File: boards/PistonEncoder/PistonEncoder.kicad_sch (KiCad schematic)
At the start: 12 parts

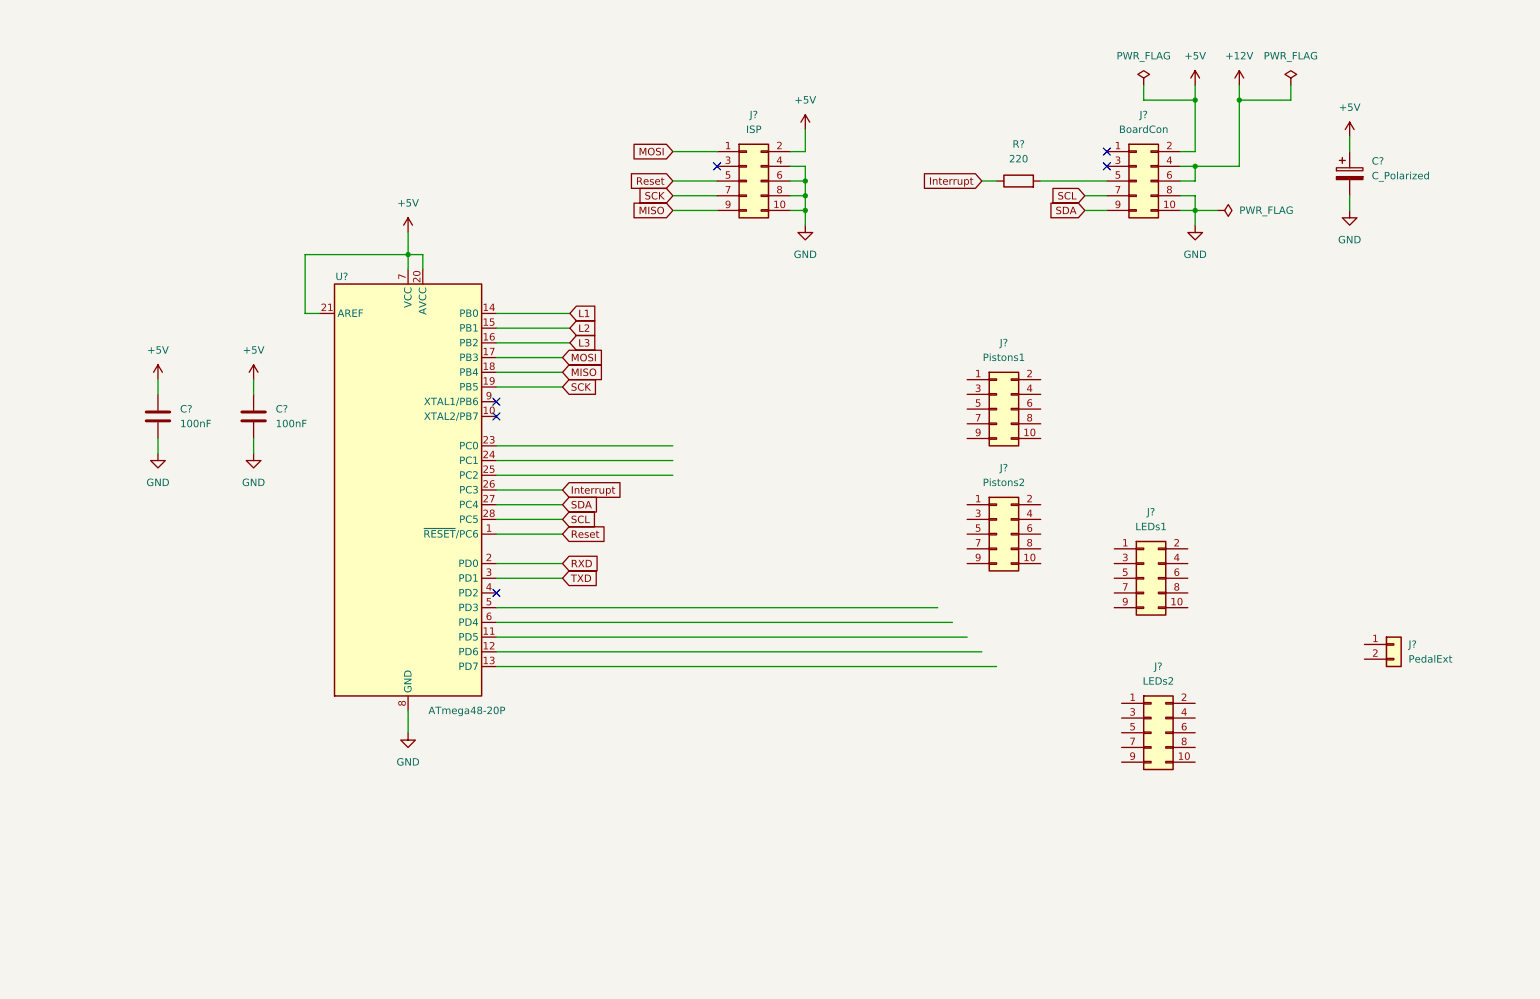
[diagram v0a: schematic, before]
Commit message: Some updates to piston encoder schematics
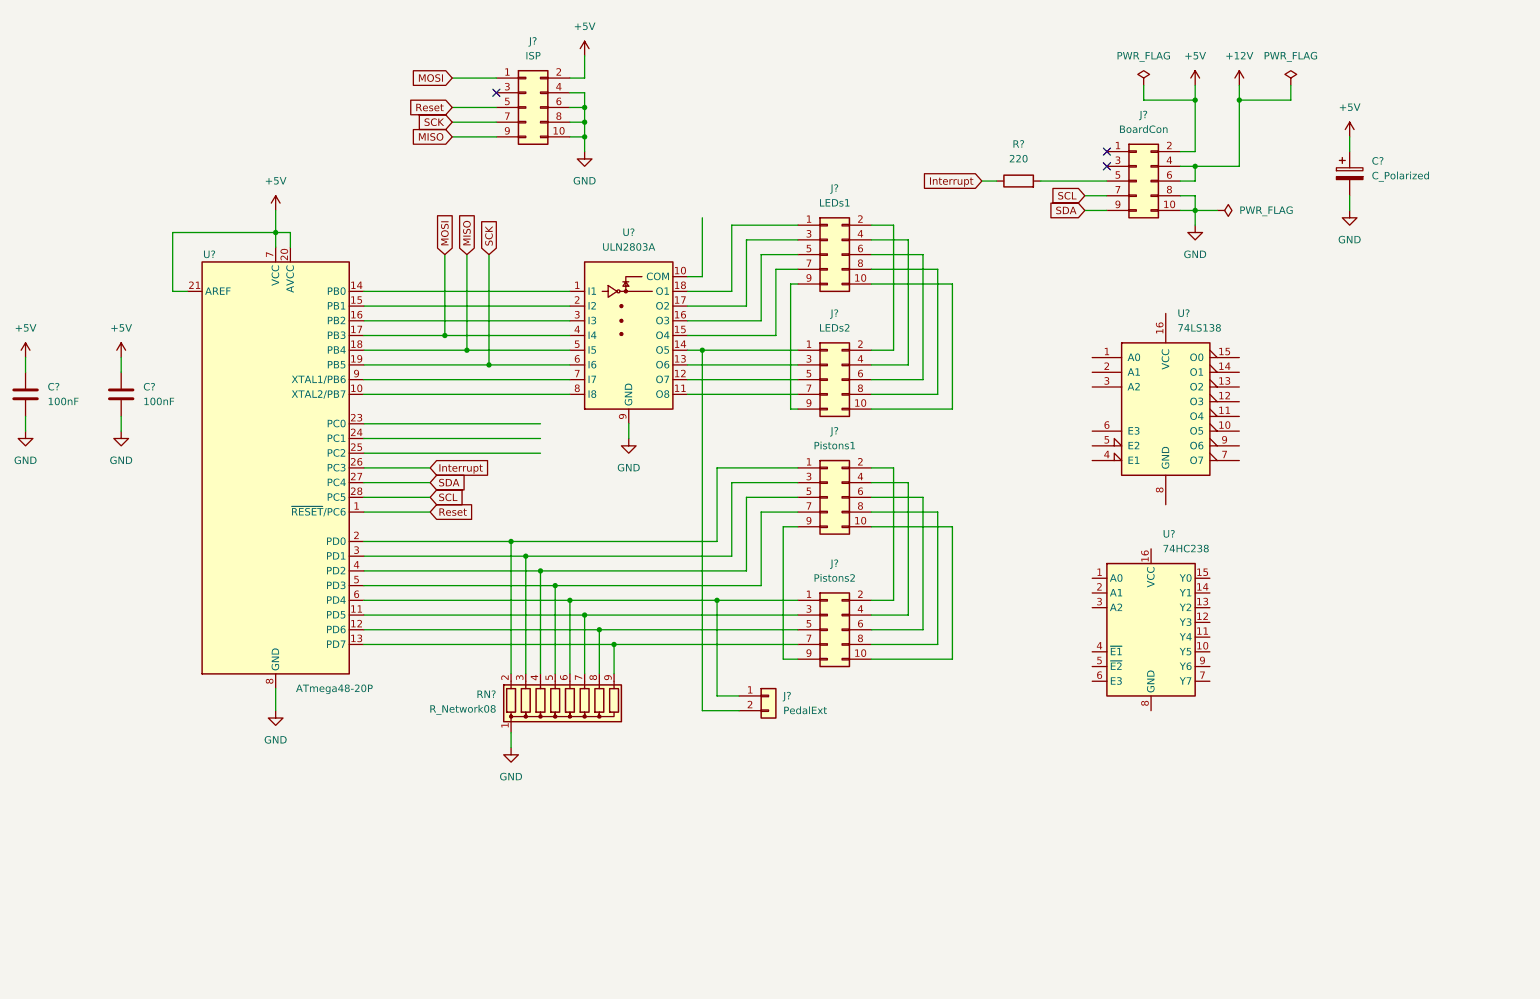
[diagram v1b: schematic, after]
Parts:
- added RN?: R_Network08, Resistor_THT:R_Array_SIP9, symbol Device:R_Network08
- added U?: ULN2803A, symbol Transistor_Array:ULN2803A
- added U?: 74HC238, symbol 74xx:74HC238
- added U?: 74LS138, symbol 74xx:74LS138
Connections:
- net RXD is gone; now on an unnamed net: U?.2 (PD0)
- net TXD is gone; now on an unnamed net: U?.3 (PD1)
- net GND: now also RN?.1 (common), U?.9 (GND)
- net MISO: now also U?.5 (I5)
- net MOSI: now also U?.4 (I4)
- net SCK: now also U?.6 (I6)
- net at J?.1 (Pin_1): now also U?.18 (O1)
- net at J?.10 (Pin_10): now also J?.10 (Pin_10) (x2)
- net at J?.2 (Pin_2): now also J?.2 (Pin_2) (x2)
- net at J?.3 (Pin_3): now also U?.17 (O2)
- net at J?.4 (Pin_4): now also J?.4 (Pin_4) (x2)
- net at J?.5 (Pin_5): now also U?.16 (O3)
- net at J?.6 (Pin_6): now also J?.6 (Pin_6) (x2)
- net at J?.7 (Pin_7): now also U?.15 (O4)
- net at J?.8 (Pin_8): now also J?.8 (Pin_8) (x2)
- net at J?.9 (Pin_9): now also J?.9 (Pin_9) (x2)
- net at J?.1 (Pin_1): now also J?.2 (Pin_2), U?.14 (O5)
- net at J?.3 (Pin_3): now also U?.13 (O6)
- net at J?.5 (Pin_5): now also U?.12 (O7)
- net at J?.7 (Pin_7): now also U?.11 (O8)
- net at U?.10 (XTAL2/PB7): now also U?.8 (I8)
- net at U?.11 (PD5): now also J?.3 (Pin_3), RN?.7 (R6)
- net at U?.12 (PD6): now also J?.5 (Pin_5), RN?.8 (R7)
- net at U?.13 (PD7): now also J?.7 (Pin_7), RN?.9 (R8)
- net at U?.4 (PD2): now also J?.5 (Pin_5), RN?.4 (R3)
- net at U?.5 (PD3): now also J?.7 (Pin_7), RN?.5 (R4)
- net at U?.6 (PD4): now also J?.1 (Pin_1), J?.1 (Pin_1), RN?.6 (R5)
- net at U?.9 (XTAL1/PB6): now also U?.7 (I7)
- net at J?.1 (Pin_1): now also RN?.2 (R1)
- net at J?.3 (Pin_3): now also RN?.3 (R2)
- net L1: no longer names the net of U?.14 (PB0)
- net L1: now also U?.1 (I1)
- net L2: no longer names the net of U?.15 (PB1)
- net L2: now also U?.2 (I2)
- net L3: no longer names the net of U?.16 (PB2)
- net L3: now also U?.3 (I3)
- no-connect marks 6 -> 3
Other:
- moved on the sheet: C?, J?, U?

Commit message: Finished Piston encoder schematics
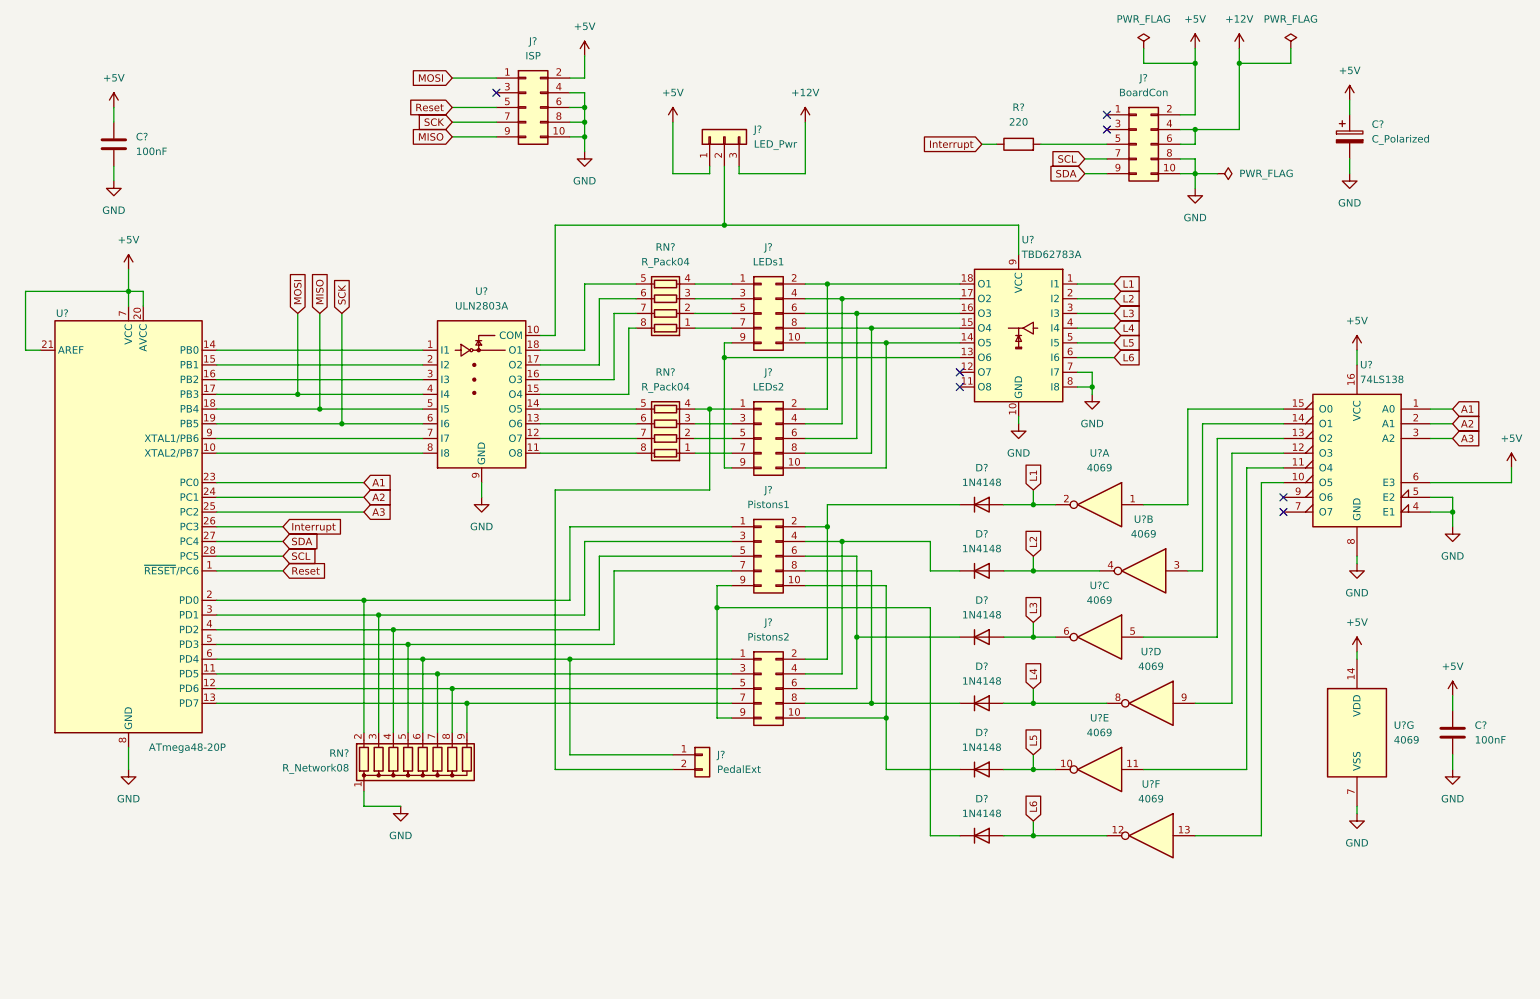
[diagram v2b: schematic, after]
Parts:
- removed U?: 74HC238, symbol 74xx:74HC238
- added D? (x6): 1N4148, Diode_THT:D_DO-35_SOD27_P7.62mm_Horizontal, symbol Diode:1N4148
- added J?: LED_Pwr, symbol Connector_Generic:Conn_01x03
- added RN? (x2): R_Pack04, symbol Device:R_Pack04
- added U? (x7): 4069, symbol 4xxx:4069
- added U?: TBD62783A, symbol Transistor_Array:TBD62783A
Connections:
- net +12V: now also J?.3 (Pin_3)
- net +5V: now also U?.16 (VCC), U?.6 (E3), J?.1 (Pin_1), U?.14 (VDD)
- net GND: now also U?.4 (E1), U?.5 (E2), U?.8 (GND), U?.10 (GND), U?.7 (I7), U?.7 (VSS), U?.8 (I8)
- net at J?.1 (Pin_1): now also RN?.4 (R4.1); no longer U?.18 (O1)
- net at J?.10 (Pin_10), J?.10 (Pin_10): now also U?.14 (O5)
- net at J?.2 (Pin_2), J?.2 (Pin_2): now also U?.18 (O1)
- net at J?.3 (Pin_3): now also RN?.3 (R3.1); no longer U?.17 (O2)
- net at J?.4 (Pin_4), J?.4 (Pin_4): now also U?.17 (O2)
- net at J?.5 (Pin_5): now also RN?.2 (R2.1); no longer U?.16 (O3)
- net at J?.6 (Pin_6), J?.6 (Pin_6): now also U?.16 (O3)
- net at J?.7 (Pin_7): now also RN?.1 (R1.1); no longer U?.15 (O4)
- net at J?.8 (Pin_8), J?.8 (Pin_8): now also U?.15 (O4)
- net at J?.9 (Pin_9), J?.9 (Pin_9): now also U?.13 (O6)
- net at U?.10 (COM): now also J?.2 (Pin_2), U?.9 (VCC)
- net at U?.11 (O8): now also RN?.8 (R1.2); no longer J?.7 (Pin_7)
- net at U?.12 (O7): now also RN?.7 (R2.2); no longer J?.5 (Pin_5)
- net at U?.13 (O6): now also RN?.6 (R3.2); no longer J?.3 (Pin_3)
- net at J?.1 (Pin_1), J?.2 (Pin_2): now also RN?.4 (R4.1); no longer U?.14 (O5)
- net A1: now reaches U?.23 (PC0)
- net A1: now also U?.1 (A0)
- net A2: now reaches U?.24 (PC1)
- net A2: now also U?.2 (A1)
- net A3: now reaches U?.25 (PC2)
- net A3: now also U?.3 (A2)
- net at J?.10 (Pin_10), J?.10 (Pin_10): now also D?.1 (K)
- net at J?.2 (Pin_2), J?.2 (Pin_2): now also D?.1 (K)
- net at J?.4 (Pin_4), J?.4 (Pin_4): now also D?.1 (K)
- net at J?.6 (Pin_6), J?.6 (Pin_6): now also D?.1 (K)
- net at J?.8 (Pin_8), J?.8 (Pin_8): now also D?.1 (K)
- net at J?.9 (Pin_9), J?.9 (Pin_9): now also D?.1 (K)
- net at U?.10 (O5): now also U?.13
- net at U?.11 (O4): now also U?.11
- net at U?.12 (O3): now also U?.9
- net at U?.13 (O2): now also U?.5
- net at U?.14 (O1): now also U?.3
- net at U?.15 (O0): now also U?.1
- new net: RN?.5 (R4.2), U?.14 (O5)
- new net: RN?.8 (R1.2), U?.15 (O4)
- new net: RN?.7 (R2.2), U?.16 (O3)
- new net: RN?.6 (R3.2), U?.17 (O2)
- new net: RN?.5 (R4.2), U?.18 (O1)
- new net: J?.3 (Pin_3), RN?.3 (R3.1)
- new net: J?.5 (Pin_5), RN?.2 (R2.1)
- new net: J?.7 (Pin_7), RN?.1 (R1.1)
- new net L1: D?.2 (A), U?.1 (I1), U?.2
- new net L2: D?.2 (A), U?.2 (I2), U?.4
- new net L3: D?.2 (A), U?.3 (I3), U?.6
- new net L4: D?.2 (A), U?.4 (I4), U?.8
- new net L5: D?.2 (A), U?.10, U?.5 (I5)
- new net L6: D?.2 (A), U?.12, U?.6 (I6)
- no-connect marks 3 -> 7
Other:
- moved on the sheet: C?, J?, R?, RN?, U?

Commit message: Renamed PCBs and updated to KiCAD 7.0
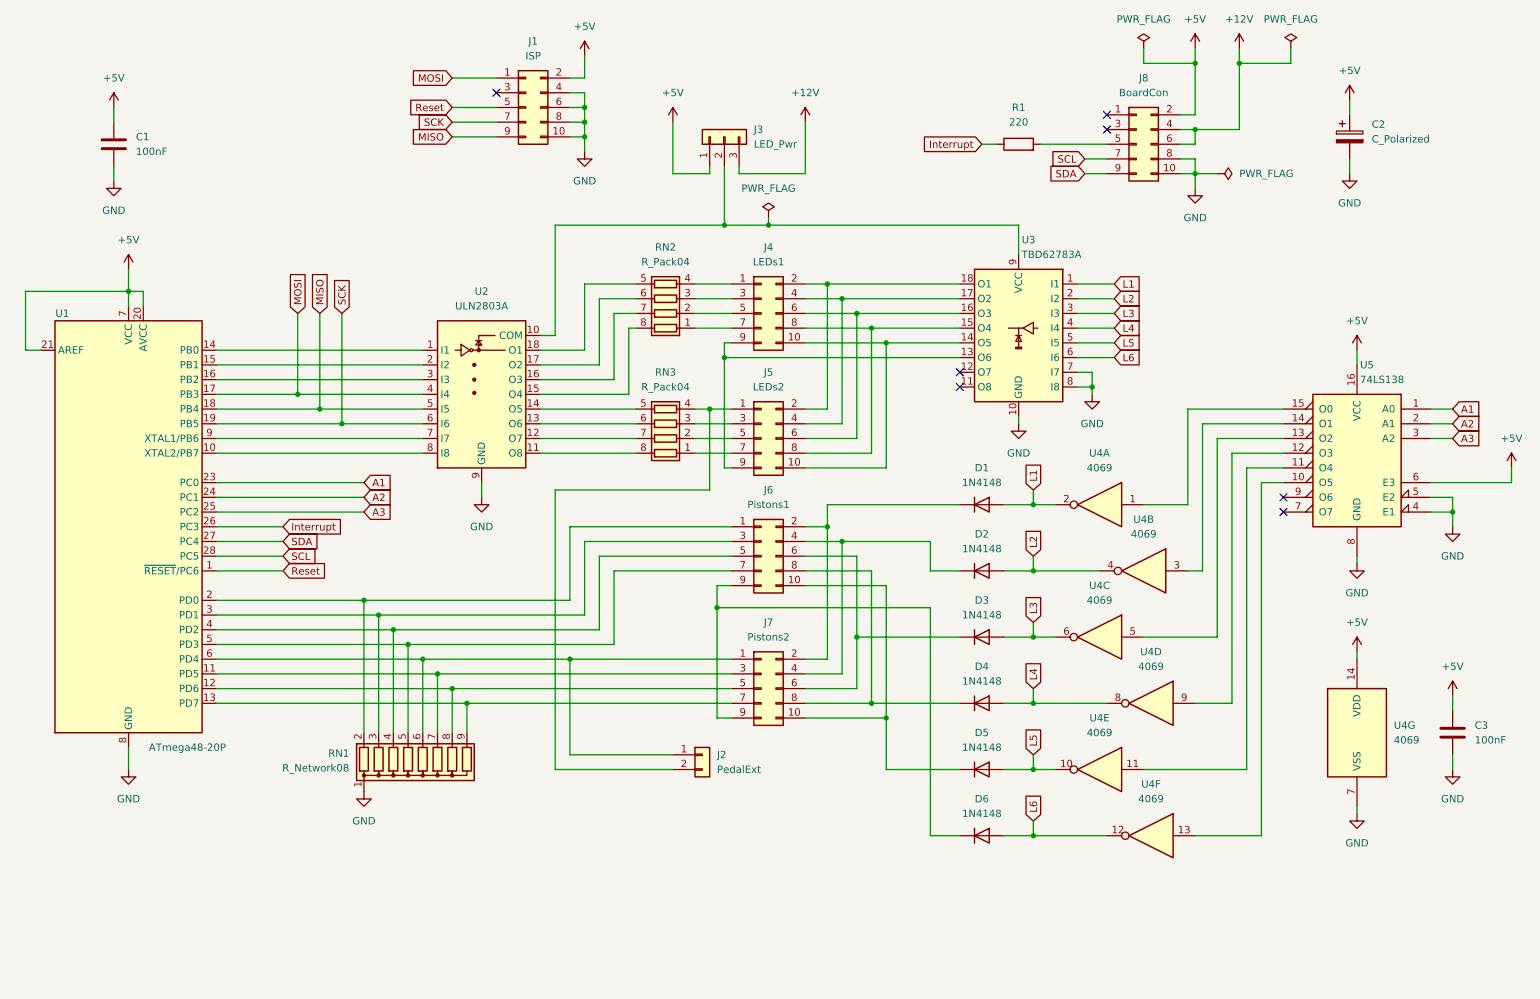
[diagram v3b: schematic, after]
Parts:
- C1: renamed from C?; footprint (none) -> Capacitor_THT:C_Disc_D7.5mm_W2.5mm_P5.00mm
- C2: renamed from C?; footprint (none) -> Capacitor_THT:CP_Radial_D10.0mm_P5.00mm
- C3: renamed from C?; footprint (none) -> Capacitor_THT:C_Radial_D6.3mm_H11.0mm_P2.50mm
- J2: renamed from J?; footprint (none) -> Connector_PinHeader_2.54mm:PinHeader_1x02_P2.54mm_Vertical
- J3: renamed from J?; footprint (none) -> Connector_PinHeader_2.54mm:PinHeader_1x03_P2.54mm_Vertical
- RN2, RN3: renamed from RN?; footprint (none) -> Resistor_THT:R_Array_SIP8
- U2, U3: renamed from U?; footprint (none) -> Package_DIP:DIP-18_W7.62mm
- U4: renamed from U?; footprint (none) -> Package_DIP:DIP-14_W7.62mm
- U5: renamed from U?; footprint (none) -> Package_DIP:DIP-16_W7.62mm
- gave numbers to parts that had none: 15
